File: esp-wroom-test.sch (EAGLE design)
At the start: 15 parts, among them U8 NCP1117LPST50T3G

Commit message: as ordered
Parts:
- removed CONN2: STEMMA_I2C_QT, 00jim:STEMMA_I2C_QT
- removed R2: (no value), 00jim:RESISTOR_0603
- added -_+_G_V_T_R_E_1: MF-CON-2.54mm-01x08, SparkFun-Connectors:M081X08
- added C4: 10uF, SparkFun-Capacitors:10UF-16V-10%(TANT)
- added D2: BAS16, SparkFun-DiscreteSemi:DIODEBAS16
- added IC1: TCAN1051HGV, microbuilder:CAN_TRANSCIEVER_TCAN1051V
- added JP1: DB9, SparkFun-Connectors:DB9FEMALE
- added POW3: (no value), MF_Passives:CAPACITOR_NP_1206
- added R10, R11: 10K, SparkFun-Resistors:10KOHM1/10W1%(0603)0603
- added R8: 200, 00jim:RESISTOR_0603
- added U1: NCP1117LPST50T3G, MF_IC_Power:NCP1117LPST50T3G
- added U2: XN04312, SparkFun-DiscreteSemi:XN04312SOT
- POW1, POW2: device MF_Passives:CAPACITOR_NP_1210 -> MF_Passives:CAPACITOR_NP_1206
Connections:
- removed net IO0: -_+_G_V_T_R_E_0.8
- removed net IO12: U$3.GPIO12
- removed net IO15: U$3.GPIO15
- removed net PD: R2.P$1
- removed net VCC1: D1.A, R1.P$2, R3.P$2, R4.P$2, R6.P$2
- new net CANRX: IC1.RXD, U$3.GPIO18
- new net CANTX: IC1.TXD, U$3.GPIO19
- new net CAN_H: IC1.CANH, JP1.1, R8.P$1
- new net CAN_L: IC1.CANL, JP1.2, R8.P$2
- new net CAN_S: IC1.S, U$3.GPIO17
- new net DB9_RX: U$3.GPIO26, U2.B2
- new net DB9_TX: R11.1, U$3.GPIO27, U2.C1
- new net N$4: C4.-, D2.A, R10.1
- new net RS-IN: D2.C, JP1.5, U2.B1
- new net RS-OUT: JP1.4, R10.2, U2.C2
- new net UNITID: -_+_G_V_T_R_E_0.1, -_+_G_V_T_R_E_1.1, JP1.3
- new net VCC_50: IC1.+5V, POW3.P$1, U1.VOUT
- net EN: now also -_+_G_V_T_R_E_1.7
- net GND: now also -_+_G_V_T_R_E_1.3, C4.+, IC1.GND, JP1.6, JP1.9, POW3.P$2, U1.GND/ADJ, U2.E1; no longer -_+_G_V_T_R_E_0.1, CONN2G$1.GND, R2.P$2
- net IO00: now also -_+_G_V_T_R_E_0.8, -_+_G_V_T_R_E_1.8
- net RAW: now also -_+_G_V_T_R_E_1.2, JP1.7, JP1.8, U1.VIN
- net RXI: now also -_+_G_V_T_R_E_1.6
- net SCL: no longer CONN2G$1.SCL
- net SDA: no longer CONN2G$1.SDA
- net TXO: now also -_+_G_V_T_R_E_1.5
- net VCC: now also -_+_G_V_T_R_E_1.4, D1.A, IC1.VIO, R1.P$2, R11.2, R3.P$2, R4.P$2, R6.P$2, U2.E2; no longer CONN2G$1.V+

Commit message: Ordered again
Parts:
- added CONN1: STEMMA_I2C_QT, 01jim:STEMMA_I2C_QT
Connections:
- net GND: now also CONN1G$1.GND
- net IO00: no longer -_+_G_V_T_R_E_0.8, -_+_G_V_T_R_E_1.8
- net SCL: now also CONN1G$1.SCL
- net SDA: now also CONN1G$1.SDA
- net VCC: now also CONN1G$1.V+
- net VCC_50: now also -_+_G_V_T_R_E_0.8, -_+_G_V_T_R_E_1.8
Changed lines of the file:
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@@
 <part name="R8" library="00jim" deviceset="RESISTOR" device="_0603" value="200"/>
 <part name="-_+_G_V_T_R_E_1" library="SparkFun-Connectors" deviceset="M08" device="1X08" value="MF-CON-2.54mm-01x08"/>
+<part name="CONN1" library="01jim" deviceset="STEMMA_I2C" device="_QT"/>
 </parts>
 <sheets>
@@
 <attribute name="NAME" x="38.1" y="107.442" size="1.778" layer="95" rot="MR0"/>
 </instance>
+<instance part="CONN1" gate="G$1" x="-55.88" y="83.82" smashed="yes">
+<attribute name="NAME" x="-59.69" y="92.075" size="1.778" layer="95"/>
+<attribute name="VALUE" x="-59.69" y="76.2" size="1.778" layer="96"/>
+</instance>
+<instance part="CONN1" gate="G$2" x="-66.04" y="96.52" smashed="yes"/>
+<instance part="CONN1" gate="G$3" x="-50.8" y="96.52" smashed="yes"/>
 </instances>
 <busses>
@@
 <wire x1="-55.88" y1="88.9" x2="-68.58" y2="88.9" width="0.1524" layer="91"/>
 <label x="-68.58" y="88.9" size="1.778" layer="95"/>
+<pinref part="CONN1" gate="G$1" pin="GND"/>
 </segment>
 <segment>
@@
 <wire x1="-55.88" y1="86.36" x2="-68.58" y2="86.36" width="0.1524" layer="91"/>
 <label x="-68.58" y="86.36" size="1.778" layer="95"/>
+<pinref part="CONN1" gate="G$1" pin="V+"/>
 </segment>
 <segment>
@@
 <label x="-104.14" y="88.9" size="1.778" layer="95"/>
 </segment>
-<segment>
-<pinref part="-_+_G_V_T_R_E_0" gate="G$1" pin="8"/>
-<wire x1="53.34" y1="104.14" x2="48.26" y2="104.14" width="0.1524" layer="91"/>
-<label x="48.26" y="104.14" size="1.778" layer="95"/>
-</segment>
-<segment>
-<pinref part="-_+_G_V_T_R_E_1" gate="G$1" pin="8"/>
-<wire x1="27.94" y1="104.14" x2="22.86" y2="104.14" width="0.1524" layer="91"/>
-<label x="22.86" y="104.14" size="1.778" layer="95"/>
-</segment>
 </net>
 <net name="IO02" class="0">
@@
 <wire x1="-55.88" y1="83.82" x2="-68.58" y2="83.82" width="0.1524" layer="91"/>
 <label x="-68.58" y="83.82" size="1.778" layer="95"/>
+<pinref part="CONN1" gate="G$1" pin="SDA"/>
 </segment>
 <segment>
@@
 <wire x1="-55.88" y1="81.28" x2="-68.58" y2="81.28" width="0.1524" layer="91"/>
 <label x="-68.58" y="81.28" size="1.778" layer="95"/>
+<pinref part="CONN1" gate="G$1" pin="SCL"/>
 </segment>
 <segment>
@@
 <pinref part="U1" gate="G$1" pin="VOUT"/>
 </segment>
-</net>
+<segment>
+<pinref part="-_+_G_V_T_R_E_1" gate="G$1" pin="8"/>
+<wire x1="27.94" y1="104.14" x2="22.86" y2="104.14" width="0.1524" layer="91"/>
+<label x="22.86" y="104.14" size="1.778" layer="95"/>
+</segment>
+<segment>
+<pinref part="-_+_G_V_T_R_E_0" gate="G$1" pin="8"/>
+<wire x1="53.34" y1="104.14" x2="48.26" y2="104.14" width="0.1524" layer="91"/>
+<label x="48.26" y="104.14" size="1.778" layer="95"/>
+</segment>
+</net>

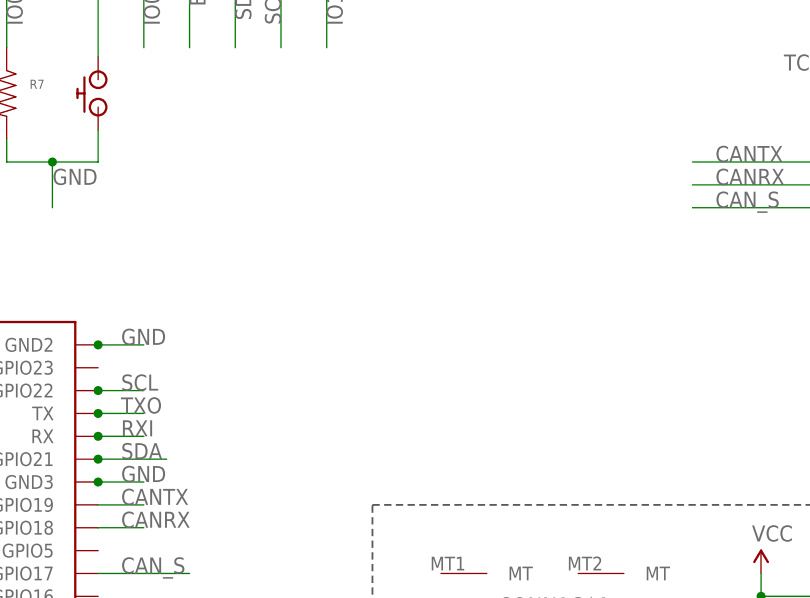
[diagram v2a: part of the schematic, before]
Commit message: Narrow board, add esp32 reset mechanism
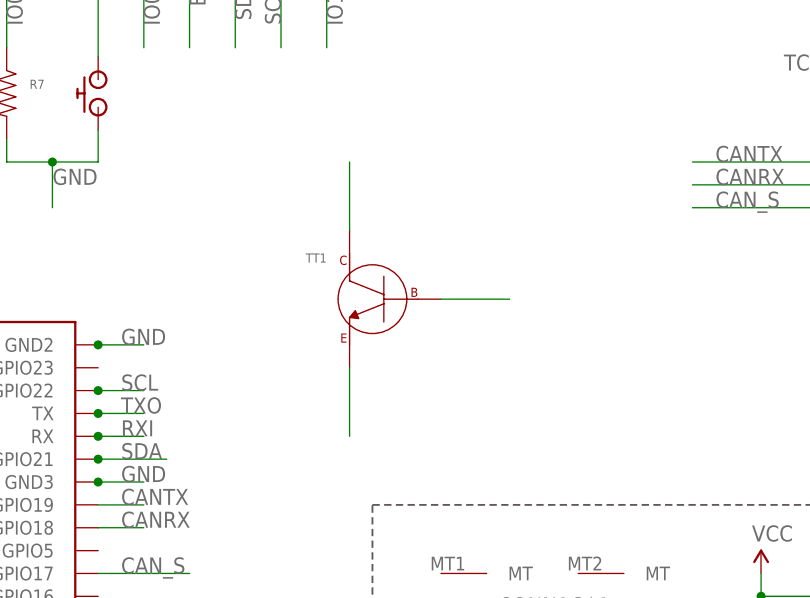
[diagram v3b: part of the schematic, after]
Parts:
- added TT1: MF-DSC-SOT233-MMBT3904, MF_Discrete_Semiconductor:NPN_BJTMMBT3904_SOT-23-3
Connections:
- new net IO21_D1: TT1.COLLECTOR
- new net N$1: TT1.EMITTER
- new net N$3: TT1.BASE
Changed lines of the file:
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@@
 <grid distance="0.1" unitdist="inch" unit="inch" style="lines" multiple="1" display="no" altdistance="0.01" altunitdist="inch" altunit="inch"/>
 <layers>
-<layer number="1" name="Top" color="4" fill="1" visible="yes" active="no"/>
-<layer number="16" name="Bottom" color="1" fill="1" visible="yes" active="no"/>
-<layer number="17" name="Pads" color="2" fill="1" visible="yes" active="no"/>
-<layer number="18" name="Vias" color="2" fill="1" visible="yes" active="no"/>
-<layer number="19" name="Unrouted" color="6" fill="1" visible="yes" active="no"/>
-<layer number="20" name="Dimension" color="24" fill="1" visible="yes" active="no"/>
-<layer number="21" name="tPlace" color="7" fill="1" visible="yes" active="no"/>
-<layer number="22" name="bPlace" color="7" fill="1" visible="yes" active="no"/>
-<layer number="23" name="tOrigins" color="15" fill="1" visible="yes" active="no"/>
-<layer number="24" name="bOrigins" color="15" fill="1" visible="yes" active="no"/>
-<layer number="25" name="tNames" color="7" fill="1" visible="yes" active="no"/>
-<layer number="26" name="bNames" color="7" fill="1" visible="yes" active="no"/>
-<layer number="27" name="tValues" color="7" fill="1" visible="yes" active="no"/>
-<layer number="28" name="bValues" color="7" fill="1" visible="yes" active="no"/>
+<layer number="1" name="Top" color="4" fill="1" visible="no" active="no"/>
+<layer number="16" name="Bottom" color="1" fill="1" visible="no" active="no"/>
+<layer number="17" name="Pads" color="2" fill="1" visible="no" active="no"/>
+<layer number="18" name="Vias" color="2" fill="1" visible="no" active="no"/>
+<layer number="19" name="Unrouted" color="6" fill="1" visible="no" active="no"/>
+<layer number="20" name="Dimension" color="24" fill="1" visible="no" active="no"/>
+<layer number="21" name="tPlace" color="7" fill="1" visible="no" active="no"/>
+<layer number="22" name="bPlace" color="7" fill="1" visible="no" active="no"/>
+<layer number="23" name="tOrigins" color="15" fill="1" visible="no" active="no"/>
+<layer number="24" name="bOrigins" color="15" fill="1" visible="no" active="no"/>
+<layer number="25" name="tNames" color="7" fill="1" visible="no" active="no"/>
+<layer number="26" name="bNames" color="7" fill="1" visible="no" active="no"/>
+<layer number="27" name="tValues" color="7" fill="1" visible="no" active="no"/>
+<layer number="28" name="bValues" color="7" fill="1" visible="no" active="no"/>
 <layer number="29" name="tStop" color="7" fill="3" visible="no" active="no"/>
 <layer number="30" name="bStop" color="7" fill="6" visible="no" active="no"/>
@@
 <layer number="35" name="tGlue" color="7" fill="4" visible="no" active="no"/>
 <layer number="36" name="bGlue" color="7" fill="5" visible="no" active="no"/>
-<layer number="37" name="tTest" color="7" fill="1" visible="yes" active="no"/>
-<layer number="38" name="bTest" color="7" fill="1" visible="yes" active="no"/>
+<layer number="37" name="tTest" color="7" fill="1" visible="no" active="no"/>
+<layer number="38" name="bTest" color="7" fill="1" visible="no" active="no"/>
 <layer number="39" name="tKeepout" color="4" fill="11" visible="no" active="no"/>
 <layer number="40" name="bKeepout" color="1" fill="11" visible="no" active="no"/>
@@
 <layer number="44" name="Drills" color="7" fill="1" visible="no" active="no"/>
 <layer number="45" name="Holes" color="7" fill="1" visible="no" active="no"/>
-<layer number="46" name="Milling" color="3" fill="1" visible="yes" active="no"/>
-<layer number="47" name="Measures" color="7" fill="1" visible="yes" active="no"/>
-<layer number="48" name="Document" color="7" fill="1" visible="yes" active="no"/>
-<layer number="49" name="Reference" color="7" fill="1" visible="yes" active="no"/>
-<layer number="50" name="dxf" color="7" fill="1" visible="yes" active="no"/>
-<layer number="51" name="tDocu" color="7" fill="1" visible="yes" active="no"/>
-<layer number="52" name="bDocu" color="7" fill="1" visible="yes" active="no"/>
-<layer number="53" name="tGND_GNDA" color="7" fill="9" visible="yes" active="no"/>
-<layer number="54" name="bGND_GNDA" color="1" fill="9" visible="yes" active="no"/>
-<layer number="56" name="wert" color="7" fill="1" visible="yes" active="no"/>
-<layer number="57" name="tCAD" color="7" fill="1" visible="yes" active="no"/>
-<layer number="58" name="b3D" color="7" fill="1" visible="yes" active="no"/>
-<layer number="59" name="tCarbon" color="7" fill="1" visible="yes" active="no"/>
-<layer number="60" name="bCarbon" color="7" fill="1" visible="yes" active="no"/>
-<layer number="61" name="stand" color="7" fill="1" visible="yes" active="no"/>
+<layer number="46" name="Milling" color="3" fill="1" visible="no" active="no"/>
+<layer number="47" name="Measures" color="7" fill="1" visible="no" active="no"/>
+<layer number="48" name="Document" color="7" fill="1" visible="no" active="no"/>
+<layer number="49" name="Reference" color="7" fill="1" visible="no" active="no"/>
+<layer number="50" name="dxf" color="7" fill="1" visible="no" active="no"/>
+<layer number="51" name="tDocu" color="7" fill="1" visible="no" active="no"/>
+<layer number="52" name="bDocu" color="7" fill="1" visible="no" active="no"/>
+<layer number="53" name="tGND_GNDA" color="7" fill="9" visible="no" active="no"/>
+<layer number="54" name="bGND_GNDA" color="1" fill="9" visible="no" active="no"/>
+<layer number="56" name="wert" color="7" fill="1" visible="no" active="no"/>
+<layer number="57" name="tCAD" color="7" fill="1" visible="no" active="no"/>
+<layer number="58" name="b3D" color="7" fill="1" visible="no" active="no"/>
+<layer number="59" name="tCarbon" color="7" fill="1" visible="no" active="no"/>
+<layer number="60" name="bCarbon" color="7" fill="1" visible="no" active="no"/>
+<layer number="61" name="stand" color="7" fill="1" visible="no" active="no"/>
 <layer number="88" name="SimResults" color="9" fill="1" visible="yes" active="yes"/>
 <layer number="89" name="SimProbes" color="9" fill="1" visible="yes" active="yes"/>
@@
 <part name="-_+_G_V_T_R_E_1" library="SparkFun-Connectors" deviceset="M08" device="1X08" value="MF-CON-2.54mm-01x08"/>
 <part name="CONN1" library="01jim" deviceset="STEMMA_I2C" device="_QT"/>
+<part name="TT1" library="MF_Discrete_Semiconductor" deviceset="NPN_BJT" device="_SOT-23-3" technology="MMBT3904" value="MF-DSC-SOT233-MMBT3904"/>
 </parts>
 <sheets>
@@
 <instance part="CONN1" gate="G$2" x="-66.04" y="96.52" smashed="yes"/>
 <instance part="CONN1" gate="G$3" x="-50.8" y="96.52" smashed="yes"/>
+<instance part="TT1" gate="G$1" x="-73.66" y="127" smashed="yes" rot="MR0">
+<attribute name="NAME" x="-78.74" y="132.08" size="1.016" layer="95" font="vector" rot="MR180" align="bottom-right"/>
+</instance>
 </instances>
 <busses>
@@
 </segment>
 </net>
+<net name="IO21_D1" class="0">
+<segment>
+<pinref part="TT1" gate="G$1" pin="COLLECTOR"/>
+<wire x1="-76.2" y1="134.62" x2="-76.2" y2="142.24" width="0.1524" layer="91"/>
+</segment>
+</net>
+<net name="N$1" class="0">
+<segment>
+<pinref part="TT1" gate="G$1" pin="EMITTER"/>
+<wire x1="-76.2" y1="119.38" x2="-76.2" y2="111.76" width="0.1524" layer="91"/>
+</segment>
+</net>
+<net name="N$3" class="0">
+<segment>
+<pinref part="TT1" gate="G$1" pin="BASE"/>
+<wire x1="-66.04" y1="127" x2="-58.42" y2="127" width="0.1524" layer="91"/>
+</segment>
+</net>

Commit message: Actually save
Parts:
- removed CONN1: STEMMA_I2C_QT, 01jim:STEMMA_I2C_QT
- removed R3, R6: (no value), 00jim:RESISTOR_0603
- removed R8: 200, 00jim:RESISTOR_0603
- added R12, R13, R2, R9: (no value), 00jim:RESISTOR_0603
- added TT2: MF-DSC-SOT233-MMBT3904, MF_Discrete_Semiconductor:NPN_BJTMMBT3904_SOT-23-3
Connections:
- removed net IO21_D1: TT1.COLLECTOR
- removed net N$1: TT1.EMITTER
- new net DTR: -_+_G_V_T_R_E_0.7, -_+_G_V_T_R_E_1.7, R9.P$1, TT1.EMITTER
- new net N$6: R9.P$2, TT2.BASE
- new net RTS: -_+_G_V_T_R_E_0.8, -_+_G_V_T_R_E_1.8, R2.P$1, TT2.EMITTER
- new net RXI_P: -_+_G_V_T_R_E_0.6, -_+_G_V_T_R_E_1.6, R13.P$1
- new net TXO_P: -_+_G_V_T_R_E_0.5, -_+_G_V_T_R_E_1.5, R12.P$1
- net CAN_H: no longer R8.P$1
- net CAN_L: no longer R8.P$2
- net EN: now also TT2.COLLECTOR; no longer -_+_G_V_T_R_E_0.7, -_+_G_V_T_R_E_1.7
- net GND: no longer CONN1G$1.GND
- net IO00: now also TT1.COLLECTOR
- net N$3: now also R2.P$2
- net RXI: now also R13.P$2; no longer -_+_G_V_T_R_E_0.6, -_+_G_V_T_R_E_1.6
- net SCL: no longer CONN1G$1.SCL, R3.P$1
- net SDA: no longer CONN1G$1.SDA, R6.P$1
- net TXO: now also R12.P$2; no longer -_+_G_V_T_R_E_0.5, -_+_G_V_T_R_E_1.5
- net VCC: no longer CONN1G$1.V+, R3.P$2, R6.P$2
- net VCC_50: no longer -_+_G_V_T_R_E_0.8, -_+_G_V_T_R_E_1.8
